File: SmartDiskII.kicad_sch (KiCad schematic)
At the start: 36 parts, among them J1 DRIVE 2, J2 DRIVE 1, J3 Apple II Expansion Slot, J4 D-SUB19 pigtail, J5 DSUB19_Socket, J6 Yellowstone pinout?, J7 DB25_Plug, U1 74LS174, U10 74LS245, U11 74LS323, U12 74LS00, U13 74LS20, U2 NE556, U3 74LS05, U4 74LS132, U5 74LS259/9334, U6 74LS21, U7 2758/16/32 P6, U8 74LS30, U9 2732

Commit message: new revision
only one drive connector, configurable with jumpers
optionally use 2764 EPROM
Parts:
- removed J1: DRIVE 2, Connector_PinHeader_2.54mm:PinHeader_2x10_P2.54mm_Vertical, symbol Connector_Generic:Conn_02x10_Odd_Even
- removed JP2: 5V on Disk 2 Pin 12, Jumper:SolderJumper-2_P1.3mm_Open_RoundedPad1.0x1.5mm, symbol Jumper:SolderJumper_2_Open
- added ALTU9: 2764, Package_DIP:DIP-28_W15.24mm, symbol Memory_EPROM:2764
- added C11, C12: .1uF, Capacitor_THT:C_Rect_L7.0mm_W2.0mm_P5.00mm, symbol Device:C_Small
- added JP4: A12H/L, Jumper:SolderJumper-3_P1.3mm_Bridged12_RoundedPad1.0x1.5mm_NumberLabels, symbol Jumper:SolderJumper_3_Bridged12
- C10: value .1uF -> 22uF; footprint Capacitor_THT:C_Rect_L7.0mm_W2.0mm_P5.00mm -> Capacitor_THT:CP_Radial_D5.0mm_P2.50mm; symbol Device:C_Small -> Device:C_Polarized_Small
- J2: value DRIVE 1 -> DRV
- renumbered J3 to J1
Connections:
- net +5V: now also ALTU9.1 (VPP), ALTU9.26 (NC), ALTU9.27 (~{PGM}), ALTU9.28 (VCC), C11.1, C12.1, JP4.3 (B)
- net A0: now also ALTU9.10 (A0)
- net A1: now also ALTU9.9 (A1)
- net A10: now also ALTU9.21 (A10)
- net A11: now also ALTU9.23 (A11)
- net A2: now also ALTU9.8 (A2)
- net A3: now also ALTU9.7 (A3)
- net A4: now also ALTU9.6 (A4)
- net A5: now also ALTU9.5 (A5)
- net A6: now also ALTU9.4 (A6)
- net A7: now also ALTU9.3 (A7)
- net A8: now also ALTU9.25 (A8)
- net A9: now also ALTU9.24 (A9)
- net GND: now also ALTU9.14 (GND), ALTU9.20 (~{CE}), C11.2, C12.2, JP4.1 (A); no longer J2.5 (Pin_5), J2.7 (Pin_7)
- net R0: now also ALTU9.11 (D0)
- net R1: now also ALTU9.12 (D1)
- net R2: now also ALTU9.13 (D2)
- net R3: now also ALTU9.15 (D3)
- net R4: now also ALTU9.16 (D4)
- net R5: now also ALTU9.17 (D5)
- net R6: now also ALTU9.18 (D6)
- net R7: now also ALTU9.19 (D7)
- net SEL1: no longer J2.12 (Pin_12), JP1.2 (B)
- net ~{ENBL 2}: now also J2.5 (Pin_5)
- net ~{ENROM}: now also ALTU9.22 (~{OE})
- new net: ALTU9.2 (A12), JP4.2 (C)
- new net SEL: J2.12 (Pin_12), JP1.2 (B)
- no-connect marks 28 -> 29

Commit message: use liron pinout with jumpers for EN2
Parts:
- added JP2: ~, Jumper:SolderJumper-2_P1.3mm_Open_RoundedPad1.0x1.5mm, symbol Jumper:SolderJumper_2_Open
- JP1: value 5V on Disk 1 Pin 12 -> ~; now in the parts list
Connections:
- net +12V: no longer J2.17 (Pin_17), J2.19 (Pin_19)
- net +5V: no longer JP1.1 (A)
- net SEL: no longer JP1.2 (B)
- net W PROT: now also J2.19 (Pin_19)
- net ~{ENBL 2}: now also JP1.1 (A), JP2.1 (A); no longer J2.5 (Pin_5)
- new net: J2.17 (Pin_17), JP1.2 (B)
- new net: J2.5 (Pin_5), JP2.2 (B)
- no-connect marks 29 -> 30

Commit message: update kicad files
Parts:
- added JP10, JP11, JP8, JP9: SolderJumper_2_Bridged, Jumper:SolderJumper-2_P1.3mm_Bridged_RoundedPad1.0x1.5mm, symbol Jumper:SolderJumper_2_Bridged
- added JP5: A13H/L, Connector_PinHeader_2.54mm:PinHeader_1x03_P2.54mm_Horizontal, symbol Connector_Generic:Conn_01x03
- added JP6: A14H/L, Connector_PinHeader_2.54mm:PinHeader_1x03_P2.54mm_Horizontal, symbol Connector_Generic:Conn_01x03
- added JP7: A15H/L, Connector_PinHeader_2.54mm:PinHeader_1x03_P2.54mm_Horizontal, symbol Connector_Generic:Conn_01x03
- added R4: 3K, Resistor_THT:R_Axial_DIN0207_L6.3mm_D2.5mm_P10.16mm_Horizontal, symbol Device:R_US
- ALTU9: symbol Memory_EPROM:2764 -> Memory_EPROM:27512
- J2: footprint Connector_PinHeader_2.54mm:PinHeader_2x10_P2.54mm_Vertical -> MyConnector:PinHeader_2x10_P2.54mm_Vertical_Shrouded
- JP4: footprint Jumper:SolderJumper-3_P1.3mm_Bridged12_RoundedPad1.0x1.5mm_NumberLabels -> Connector_PinHeader_2.54mm:PinHeader_1x03_P2.54mm_Horizontal; symbol Jumper:SolderJumper_3_Bridged12 -> Connector_Generic:Conn_01x03
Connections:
- net +5V: now also JP4.1 (Pin_1), JP10.2 (B), JP11.2 (B), JP5.1 (Pin_1), JP6.1 (Pin_1), JP7.1 (Pin_1), JP8.2 (B), JP9.2 (B), R4.1; no longer ALTU9.1 (VPP), ALTU9.26 (NC), ALTU9.27 (~{PGM}), JP4.3 (B), U9.24 (VCC)
- net GND: now also JP4.3 (Pin_3), JP5.3 (Pin_3), JP6.3 (Pin_3), JP7.3 (Pin_3); no longer JP4.1 (A)
- net FWA12: now reaches ALTU9.2 (A12), JP4.2 (Pin_2)
- net FWA12: now also JP8.1 (A)
- net at U3.10, U3.9, U7.18 (~{CE}): now also R4.2
- new net FWA13: ALTU9.26 (A13), JP5.2 (Pin_2), JP9.1 (A), U9.24 (VCC)
- new net FWA14: ALTU9.27 (A14), JP10.1 (A), JP6.2 (Pin_2)
- new net FWA15: ALTU9.1 (A15), JP11.1 (A), JP7.2 (Pin_2)
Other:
- note added: "CA1"
- note added: "CA2"
- note added: "ENABLE (MOTOR)"
- note added: "L6/Q6"
- note added: "L7/Q7"
- note added: "LSTRB"
- note added: "REQ/CA0"
- note removed: "L6"
- note removed: "L7"
- moved on the sheet: ALTU9

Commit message: rev2
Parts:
- removed JP10, JP11, JP8, JP9: SolderJumper_2_Bridged, Jumper:SolderJumper-2_P1.3mm_Bridged_RoundedPad1.0x1.5mm, symbol Jumper:SolderJumper_2_Bridged
- removed JP4: A12H/L, Connector_PinHeader_2.54mm:PinHeader_1x03_P2.54mm_Horizontal, symbol Connector_Generic:Conn_01x03
- removed JP5: A13H/L, Connector_PinHeader_2.54mm:PinHeader_1x03_P2.54mm_Horizontal, symbol Connector_Generic:Conn_01x03
- removed JP6: A14H/L, Connector_PinHeader_2.54mm:PinHeader_1x03_P2.54mm_Horizontal, symbol Connector_Generic:Conn_01x03
- removed JP7: A15H/L, Connector_PinHeader_2.54mm:PinHeader_1x03_P2.54mm_Horizontal, symbol Connector_Generic:Conn_01x03
- added C13, C14: 100n, Capacitor_THT:C_Disc_D4.3mm_W1.9mm_P5.00mm, symbol Device:C_Small
- added JP3: ~, Jumper:SolderJumper-2_P1.3mm_Open_RoundedPad1.0x1.5mm, symbol Jumper:SolderJumper_2_Open
- added JP5, JP6, JP7: ~, Connector_PinHeader_2.54mm:PinHeader_1x02_P2.54mm_Vertical, symbol Jumper:Jumper_2_Bridged
- added R5, R6, R7, R8: 10K, Resistor_THT:R_Axial_DIN0207_L6.3mm_D2.5mm_P10.16mm_Horizontal, symbol Device:R_US
- added SJP10, SJP8, SJP9: ~, Jumper:SolderJumper-2_P1.3mm_Bridged_RoundedPad1.0x1.5mm, symbol Jumper:SolderJumper_2_Bridged
- ALTU10: renamed from ALTU9; value 2764 -> '64-'512; symbol Memory_EPROM:27512 -> Memory_EEPROM:28C256
- C1: renamed from C4; value 22uF -> 22u
- C10: renamed from C2; value .1uF -> 100n; footprint Capacitor_THT:C_Rect_L7.0mm_W2.0mm_P5.00mm -> Capacitor_THT:C_Disc_D4.3mm_W1.9mm_P5.00mm
- C11, C12, C3, C5, C6, C7, C8, C9: value .1uF -> 100n; footprint Capacitor_THT:C_Rect_L7.0mm_W2.0mm_P5.00mm -> Capacitor_THT:C_Disc_D4.3mm_W1.9mm_P5.00mm
- C2: renamed from C10; value 22uF -> 22u
- C4: renamed from C1; value .1uF -> 100n; footprint Capacitor_THT:C_Rect_L7.0mm_W2.0mm_P5.00mm -> Capacitor_THT:C_Disc_D4.3mm_W1.9mm_P5.00mm
- renumbered JP2 to JP1, JP1 to JP2, JP3 to JP4, U9 to U10, U10 to U11, U11 to U12, U12 to U13, U13 to U6, U6 to U7, U7 to U8, U8 to U9
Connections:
- net FWA12 is gone; now on net GND: ALTU10.2 (A12)
- net FWA13 is gone; now on net +5V: ALTU10.26 (A13), U10.24 (VCC)
- net FWA14 is gone; now on net +5V: ALTU10.27 (~{WE})
- net PH0 is gone; now on net PHASE0: J6.2 (Pin_2)
- net PH1 is gone; now on net PHASE1: J6.4 (Pin_4)
- net PH2 is gone; now on net PHASE2: J6.6 (Pin_6)
- net PH3 is gone; now on net PHASE3: J6.8 (Pin_8)
- net +12V: now also C12.1, C8.1; no longer C6.1, C7.1
- net +5V: now also C6.1, C7.1, C9.2, C13.1, R8.1; no longer C12.1, C8.1
- net -12V: now also C14.2; no longer C9.1
- net A10: now also JP7.1 (A), SJP10.1 (A); no longer ALTU10.21 (A10), U10.19 (A10)
- net A8: now also JP5.1 (A), SJP8.1 (A); no longer ALTU10.25 (A8), U10.23 (A8)
- net A9: now also JP6.1 (A), SJP9.1 (A); no longer ALTU10.24 (A9), U10.22 (A9)
- net GND: now also C9.1, C13.2, C14.1, R5.1, R6.1, R7.1; no longer C9.2
- net W PROT: now also JP3.2 (B); no longer J2.19 (Pin_19)
- net FWA15: no longer names the net of ALTU10.1 (A14)
- net FWA15: now also R8.2
- new net: J2.19 (Pin_19), JP3.1 (A)
- new net FWA10: ALTU10.21 (A10), JP7.2 (B), R7.2, SJP10.2 (B), U10.19 (A10)
- new net FWA8: ALTU10.25 (A8), JP5.2 (B), R5.2, SJP8.2 (B), U10.23 (A8)
- new net FWA9: ALTU10.24 (A9), JP6.2 (B), R6.2, SJP9.2 (B), U10.22 (A9)
- no-connect marks 30 -> 31
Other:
- moved on the sheet: ALTU10, C10, C11, C12, C2, C4, C6, C7, C8, C9, R4

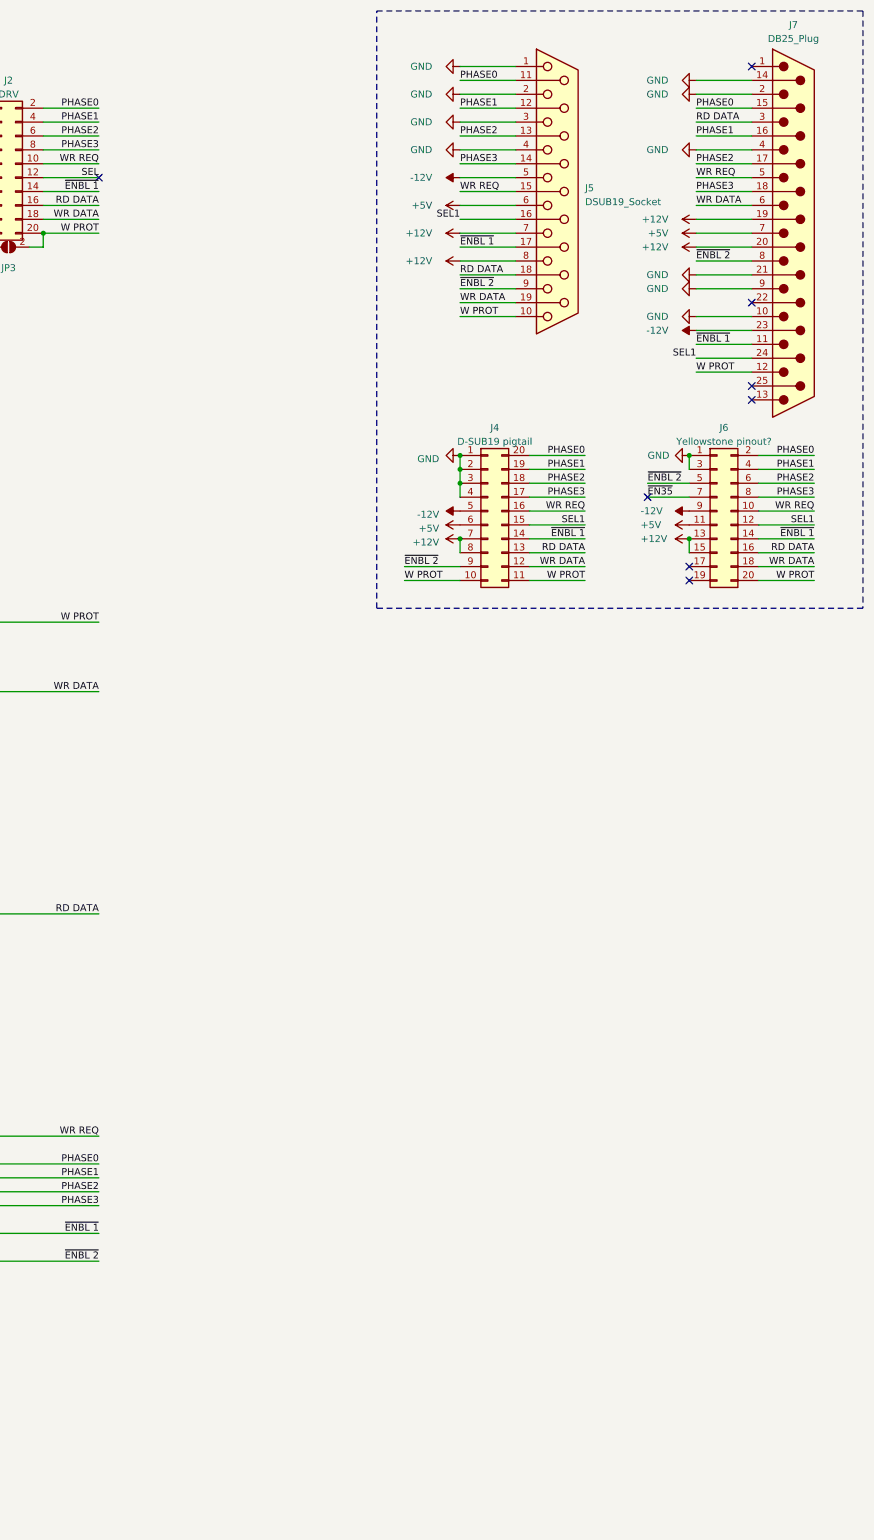
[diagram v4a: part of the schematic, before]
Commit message: add page for cables
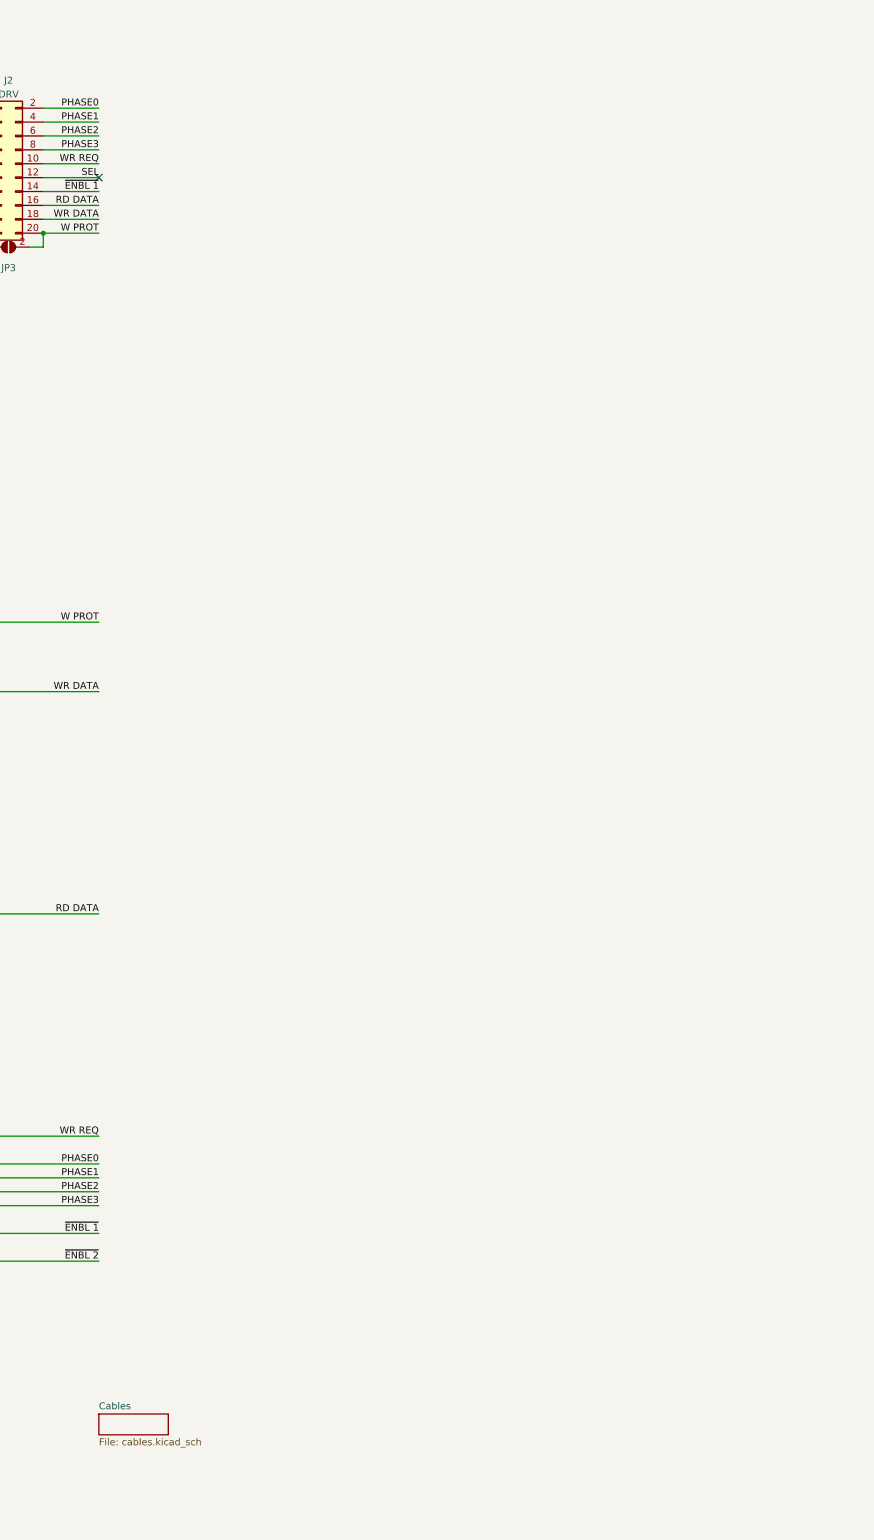
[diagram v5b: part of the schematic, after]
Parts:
- removed J4: D-SUB19 pigtail, Package_DIP:DIP-20_W7.62mm, symbol Connector_Generic:Conn_02x10_Counter_Clockwise
- removed J5: DSUB19_Socket, symbol MyConnector:DSUB19_Female
- removed J6: Yellowstone pinout?, Connector_PinHeader_2.54mm:PinHeader_2x10_P2.54mm_Horizontal, symbol Connector_Generic:Conn_02x10_Odd_Even
- removed J7: DB25_Plug, symbol Connector:DB25_Plug
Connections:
- no-connect marks 31 -> 24
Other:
- added sheet Cables (cables.kicad_sch)

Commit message: All slot auto-switching rom
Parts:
- removed ALTU10: '64-'512, Package_DIP:DIP-28_W15.24mm, symbol Memory_EEPROM:28C256
- removed JP5, JP6, JP7: ~, Connector_PinHeader_2.54mm:PinHeader_1x02_P2.54mm_Vertical, symbol Jumper:Jumper_2_Bridged
- removed R5, R6, R7, R8: 10K, Resistor_THT:R_Axial_DIN0207_L6.3mm_D2.5mm_P10.16mm_Horizontal, symbol Device:R_US
- removed SJP10, SJP8, SJP9: ~, Jumper:SolderJumper-2_P1.3mm_Bridged_RoundedPad1.0x1.5mm, symbol Jumper:SolderJumper_2_Bridged
- removed U10: 2732, Package_DIP:DIP-24_W15.24mm, symbol MyEprom:2732
- added JP5, JP6: ~, Jumper:SolderJumper-3_P1.3mm_Bridged12_RoundedPad1.0x1.5mm_NumberLabels, symbol Jumper:SolderJumper_3_Bridged12
- added JP8: ~, Connector_PinHeader_2.54mm:PinHeader_1x02_P2.54mm_Vertical, symbol Jumper:Jumper_2_Bridged
- added R10: 10K, Resistor_THT:R_Axial_DIN0207_L6.3mm_D2.5mm_P10.16mm_Horizontal, symbol Device:R_US
- added U10: 27C256, Package_DIP:DIP-28_W15.24mm, symbol Memory_EPROM:27C256
- added U14: 74LS174, Package_DIP:DIP-16_W7.62mm, symbol 74xx:74LS174
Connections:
- net +5V: now also JP5.3 (B), JP6.3 (B), R10.2, U10.28 (VCC), U14.16 (VCC)
- net A0: now also U10.10 (A0)
- net A1: now also U10.9 (A1)
- net A10: now also U10.21 (A10), U14.14 (D5)
- net A11: now also U10.23 (A11)
- net A2: now also U10.8 (A2)
- net A3: now also U10.7 (A3)
- net A4: now also U10.6 (A4)
- net A5: now also U10.5 (A5)
- net A6: now also U10.4 (A6)
- net A7: now also U10.3 (A7)
- net A8: now also U10.25 (A8), U14.11 (D3)
- net A9: now also U10.24 (A9), U14.13 (D4)
- net ENCOMMON: now also U14.9 (Cp)
- net GND: now also JP8.1 (A), U10.14 (GND), U10.20 (~{CE}), U14.8 (GND)
- net R0: now also U10.11 (D0)
- net R1: now also U10.12 (D1)
- net R2: now also U10.13 (D2)
- net R3: now also U10.15 (D3)
- net R4: now also U10.16 (D4)
- net R5: now also U10.17 (D5)
- net R6: now also U10.18 (D6)
- net R7: now also U10.19 (D7)
- net ~{ENROM}: now also U10.22 (~{OE})
- net A12: now reaches J1.14 (Pin_14)
- net A13: now reaches J1.15 (Pin_15)
- net A14: now reaches J1.16 (Pin_16)
- new net: JP8.2 (B), R10.1, U14.1 (~{Mr})
- new net: JP6.2 (C), U10.1 (VPP)
- new net: JP5.2 (C), U10.27 (A14)
- new net LA12: U10.2 (A12), U14.10 (Q3)
- new net LA13: U10.26 (A13), U14.12 (Q4)
- new net LA14: JP5.1 (A), JP6.1 (A), U14.15 (Q5)
- no-connect marks 24 -> 27
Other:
- note added: "28C256 needs pins 1 and 27 reversed"
- note added: "Rising ENCOMMON will set FW12-14 equal to A8-10, selecting region of ROM specific to slot. so access to CN00 selects rom region N000 When jumper holds pin 1 low, region 0000 is selected, which will be the Disk II firmware, repeated at 0100, 0200, 0300, etc)"
- moved on the sheet: J1, J2, JP1, JP2, JP3
